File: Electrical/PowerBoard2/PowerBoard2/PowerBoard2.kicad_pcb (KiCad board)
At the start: 2 copper layers, 30 parts, among them U1 LMZ22005TZ/NOPB, U2 INA226AIDGSR, U4 TLV2370IDBVR, U5 TLV2370IDBVR

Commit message: pads
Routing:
- net /Buck Converter/Vin (12V): track 7.75 -> 14.7 mm
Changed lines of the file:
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@@
 	(footprint "Capacitor_SMD:C_0805_2012Metric_Pad1.18x1.45mm_HandSolder"
 		(layer "F.Cu")
-		(at 130.8 88.7375 90)
+		(at 130.8 88.75 90)
 		(descr "Capacitor SMD 0805 (2012 Metric), square (rectangular) end terminal, IPC_7351 nominal with elongated pad for handsoldering. (Body size source: IPC-SM-782 page 76, https://www.pcb-3d.com/wordpress/wp-content/uploads/ipc-sm-782a_amendment_1_and_2.pdf, https://docs.google.com/spreadsheets/d/1BsfQQcO9C6DZCsRaXUlFlo91Tg2WpOkGARC1WS5S8t0/edit?usp=sharing), generated with kicad-footprint-generator")
 		(tags "capacitor handsolder")
@@
 	(footprint "Capacitor_SMD:C_0805_2012Metric_Pad1.18x1.45mm_HandSolder"
 		(layer "F.Cu")
-		(at 128.2 88.7625 90)
+		(at 128.2 88.75 90)
 		(descr "Capacitor SMD 0805 (2012 Metric), square (rectangular) end terminal, IPC_7351 nominal with elongated pad for handsoldering. (Body size source: IPC-SM-782 page 76, https://www.pcb-3d.com/wordpress/wp-content/uploads/ipc-sm-782a_amendment_1_and_2.pdf, https://docs.google.com/spreadsheets/d/1BsfQQcO9C6DZCsRaXUlFlo91Tg2WpOkGARC1WS5S8t0/edit?usp=sharing), generated with kicad-footprint-generator")
 		(tags "capacitor handsolder")
@@
 	)
 	(segment
-		(start 135.6 67.5)
-		(end 135.6 70.3)
+		(start 128.6939 72.1061)
+		(end 128.6939 71.2)
 		(width 0.2)
 		(layer "F.Cu")
@@
 	)
 	(segment
-		(start 128.6939 72.1061)
-		(end 128.6939 71.2)
+		(start 128.6939 71.2)
+		(end 128.6939 69.0061)
 		(width 0.2)
 		(layer "F.Cu")
@@
 	)
 	(segment
+		(start 128.6939 69.0061)
+		(end 130.2 67.5)
+		(width 0.2)
+		(layer "F.Cu")
+		(net 2)
+	)
+	(segment
 		(start 127 74.85)
 		(end 127 73.8)
@@
 	)
 	(segment
+		(start 130.2 67.5)
+		(end 135.6 67.5)
+		(width 0.2)
+		(layer "F.Cu")
+		(net 2)
+	)
+	(segment
 		(start 149.6 76.307201)
 		(end 149.6 79.45)
@@
 	(segment
 		(start 140.7648 65.6)
-		(end 141.7 65.6)
+		(end 141.6 65.6)
 		(width 0.2)
 		(layer "F.Cu")
@@
 	)
 	(segment
-		(start 141.7 65.6)
-		(end 141.9 65.8)
+		(start 141.9 65.9)
+		(end 141.9 67.25)
 		(width 0.2)
 		(layer "F.Cu")
@@
 	)
 	(segment
-		(start 142.075002 67.500002)
+		(start 142.150002 67.500002)
 		(end 143 67.500002)
 		(width 0.2)
@@
 	)
 	(segment
-		(start 144.8 61.3)
-		(end 140.7648 65.3352)
+		(start 141.6 65.6)
+		(end 141.9 65.9)
 		(width 0.2)
 		(layer "F.Cu")
@@
 	)
 	(segment
-		(start 141.9 67.325)
-		(end 142.075002 67.500002)
+		(start 144.8 61.3)
+		(end 140.7648 65.3352)
 		(width 0.2)
 		(layer "F.Cu")
@@
 	)
 	(segment
-		(start 141.9 65.8)
-		(end 141.9 67.325)
+		(start 141.9 67.25)
+		(end 142.150002 67.500002)
 		(width 0.2)
 		(layer "F.Cu")
@@
 	)
 	(segment
-		(start 151.3648 65.6)
-		(end 151.3648 65.3648)
+		(start 152.4824 65.875001)
+		(end 152.4824 67.225001)
 		(width 0.2)
 		(layer "F.Cu")
@@
 	)
 	(segment
-		(start 152.3014 65.6)
-		(end 152.5 65.7986)
+		(start 151.3648 65.6)
+		(end 151.3648 65.3648)
 		(width 0.2)
 		(layer "F.Cu")
@@
 	)
 	(segment
-		(start 152.5 67.336602)
-		(end 152.6634 67.500002)
+		(start 152.1824 65.575001)
+		(end 152.4824 65.875001)
 		(width 0.2)
 		(layer "F.Cu")
@@
 	)
 	(segment
-		(start 152.5 65.7986)
-		(end 152.5 67.336602)
+		(start 151.3472 65.575001)
+		(end 152.1824 65.575001)
 		(width 0.2)
 		(layer "F.Cu")
@@
 	)
 	(segment
-		(start 151.3648 65.6)
-		(end 152.3014 65.6)
+		(start 151.3648 65.3648)
+		(end 147.3 61.3)
 		(width 0.2)
 		(layer "F.Cu")
@@
 	)
 	(segment
-		(start 151.3648 65.3648)
-		(end 147.3 61.3)
+		(start 152.757401 67.500002)
+		(end 153.6 67.500002)
 		(width 0.2)
 		(layer "F.Cu")
@@
 	)
 	(segment
-		(start 152.6634 67.500002)
-		(end 153.6 67.500002)
+		(start 152.4824 67.225001)
+		(end 152.757401 67.500002)
 		(width 0.2)
 		(layer "F.Cu")
@@
 		(polygon
 			(pts
-				(xy 154.5 81.5) (xy 160.5 81.5) (xy 162.6 79.4) (xy 162.6 77.4) (xy 161.2 76) (xy 159.5 76) (xy 153.3 69.8)
+				(xy 154.2 81.7) (xy 160.5 81.7) (xy 162.6 79.4) (xy 162.6 77.4) (xy 161.2 76) (xy 159.5 76) (xy 153.3 69.8)
 				(xy 127.8 69.8) (xy 127.8 72.6) (xy 130.9 72.6) (xy 135.8 77.5) (xy 140.5 77.5) (xy 143.5 74.5)
-				(xy 152.5 74.5) (xy 154.5 76.5)
+				(xy 152.5 74.5) (xy 154.2 76.5)
 			)
 		)
@@
 		(layer "F.Cu")
 		(hatch edge 0.5)
-		(priority 4)
 		(connect_pads yes
 			(clearance 0)
@@
 		(polygon
 			(pts
-				(xy 114.5 89.2) (xy 114.5 90.3) (xy 117.1 90.3) (xy 139.5 95.975003) (xy 139.5 93.5) (xy 139.5 90)
-				(xy 131.75 89.2)
+				(xy 147.5 81.7) (xy 147.5 78.9) (xy 145.3 76.8) (xy 145.3 75.6) (xy 144.3 75.6) (xy 141.5 78.4)
+				(xy 141.5 82.4) (xy 139 84.8) (xy 139 98) (xy 141.8 98) (xy 144.9 94.4) (xy 144.9 83.4)
 			)
 		)
@@
 		(layer "F.Cu")
 		(hatch edge 0.5)
+		(priority 1)
 		(connect_pads yes
 			(clearance 0)
@@
 		(polygon
 			(pts
-				(xy 139 98) (xy 141.5 98) (xy 145 94.5) (xy 145 83.5) (xy 146.8 81.7) (xy 147.5 81.7) (xy 147.5 79)
-				(xy 146 77.623433) (xy 145.348002 77) (xy 145.348002 76.5) (xy 145.348002 75.550801) (xy 143.949199 75.550801)
-				(xy 141.5 78) (xy 141.5 85.5) (xy 139 87.9)
+				(xy 141.8 98) (xy 142.9 99.4) (xy 160.96 99.4) (xy 162.6 98.1) (xy 162.6 95.6) (xy 160.849998 94.4)
+				(xy 144.9 94.4)
 			)
 		)
@@
 		(layer "F.Cu")
 		(hatch edge 0.5)
-		(priority 1)
+		(priority 4)
 		(connect_pads yes
 			(clearance 0)
@@
 		(polygon
 			(pts
-				(xy 141.25 97.75) (xy 142.9 99.4) (xy 160.96 99.4) (xy 162.6 98.1) (xy 162.6 95.6) (xy 160.849998 94.4)
-				(xy 144.6 94.4)
+				(xy 114.3 90.4) (xy 117.5 90.4) (xy 120.2 93.1) (xy 124 93.1) (xy 139 96) (xy 139 90) (xy 131.8 89.1)
+				(xy 114.3 89.1)
 			)
 		)

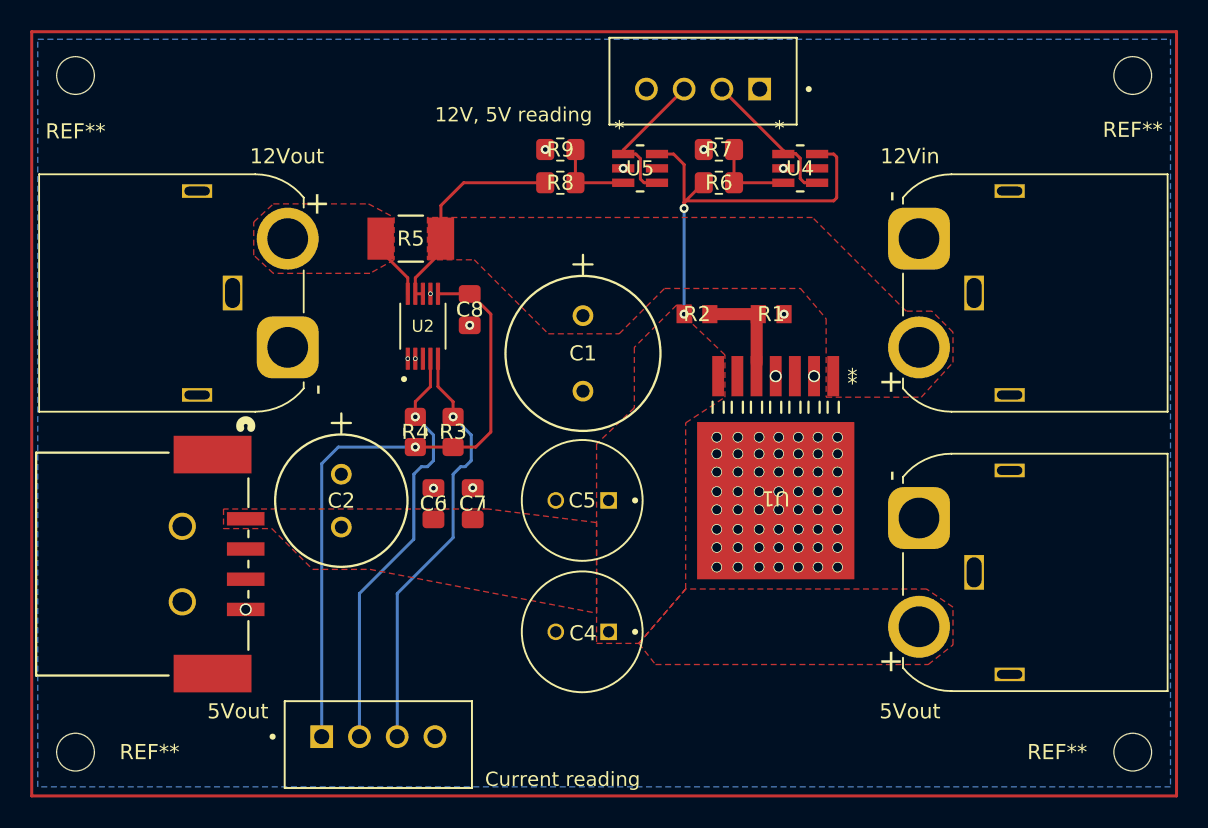
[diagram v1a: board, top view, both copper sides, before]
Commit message: Updated Board to use two INA226
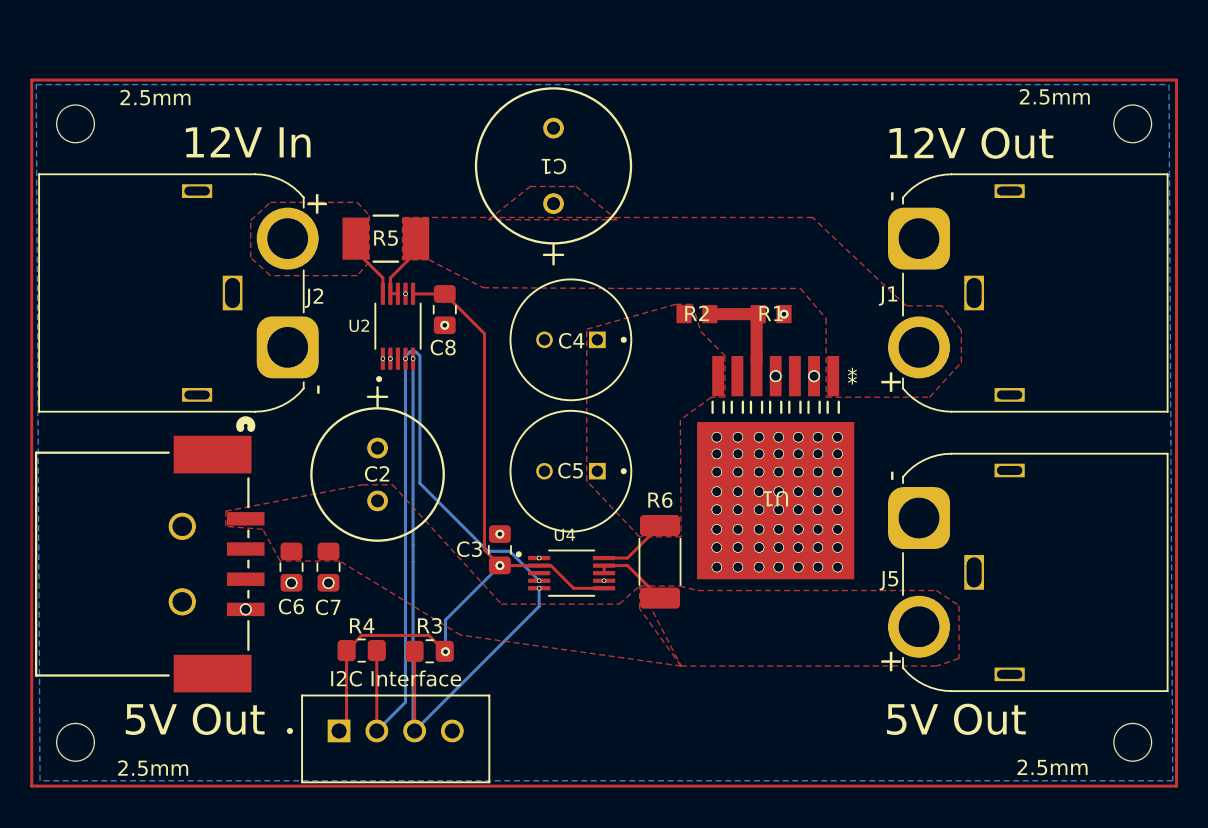
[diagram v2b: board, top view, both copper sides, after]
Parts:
- removed 12V, 5V reading: B4B-XH-A_LF__SN_, B4B-XH-A_LF__SN_:JST_B4B-XH-A_LF__SN_
- removed R7, R9: 33k, Resistor_SMD:R_0805_2012Metric_Pad1.20x1.40mm_HandSolder
- removed R8: 120k, Resistor_SMD:R_0805_2012Metric_Pad1.20x1.40mm_HandSolder
- removed REF** (x2): MountingHole_2.5mm, MountingHole:MountingHole_2.5mm
- removed U5: TLV2370IDBVR, _Footprints:DBV6
- added 2.5mm: MountingHole_2.5mm, MountingHole:MountingHole_2.5mm, F.Cu at (174.5, 63.6)
- added 2.5mm: MountingHole_2.5mm, MountingHole:MountingHole_2.5mm, F.Cu at (104.5, 63.6)
- added C3: 0.1uF, Capacitor_SMD:C_0805_2012Metric_Pad1.18x1.45mm_HandSolder, F.Cu at (132.6, 91.8)
- 5V Out: renamed from 5Vout
- I2C Interface: renamed from Current reading
- R6: value 36k -> CSNL2010FT2L00; footprint Resistor_SMD:R_0805_2012Metric_Pad1.20x1.40mm_HandSolder -> Resistor_SMD:R_2010_5025Metric_Pad1.40x2.65mm_HandSolder
- U4: value TLV2370IDBVR -> INA226AIDGSR; footprint _Footprints:DBV6 -> Libraries:INA226AIDGSR
- moved U4 30.8 mm to (137.3, 93.3)
- moved R6 25.4 mm to (143.2, 92.6), turned to 90 degrees
- moved C4 19.3 mm to (137.3, 77.9)
- moved R4 14.9 mm to (123.5, 98.5), turned to 0 degrees
- moved R3 14.6 mm to (128.0, 98.5), turned to 180 degrees
- moved C7 10.4 mm to (121.2, 93.0), turned to -90 degrees
- moved C6 10.3 mm to (118.8, 93.0), turned to -90 degrees
- moved C1 7.67 mm to (136.2, 68.9), turned to 90 degrees
- moved C2 2.96 mm to (124.5, 85.1)
- moved C5 2.07 mm to (137.3, 86.6)
- moved C8 1.65 mm to (128.9, 75.9)
- moved R5 1.65 mm to (125.0, 71.2)
- moved U2 1.65 mm to (125.8, 77.0)
- moved I2C Interface 1.21 mm to (125.7, 104.3)
- moved 2.5mm 0.65 mm to (104.5, 104.5)
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- renumbered REF** to 2.5mm, 12Vin to J1, 12Vout to J2, 5Vout to J5
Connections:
- C1 pad 1: /Buck Converter/Vin (12V) -> +12V
- C4 pad 1: +5V -> /Buck Converter/Vout (5V 5A)
- C5 pad 1: +5V -> /Buck Converter/Vout (5V 5A)
- J1 pad 2: /Buck Converter/Vin (12V) -> +12V
- J2 pad 2: +12V -> Net-(J2--)
- R2 pad 1: +5V -> /Buck Converter/Vout (5V 5A)
- R5 pad 1: +12V -> Net-(J2--)
- R5 pad 2: /Buck Converter/Vin (12V) -> +12V
- R6 pad 2: Net-(U4-IN+) -> /Buck Converter/Vout (5V 5A)
- U1 pad 1: /Buck Converter/Vin (12V) -> +12V
- U1 pad 7: +5V -> /Buck Converter/Vout (5V 5A)
- U2 pad 10: +12V -> Net-(J2--)
- U2 pad 8: /Buck Converter/Vin (12V) -> +12V
- U2 pad 9: /Buck Converter/Vin (12V) -> +12V
- U4 pad 1: Net-(U4-IN-) -> GND
- U4 pad 2: GND -> +3.3V
- U4 pad 3: Net-(U4-IN+) -> unconnected-(U4-ALERT-Pad3)
- U4 pad 4: Net-(U4-IN-) -> /SDA
- U4 pad 5: unconnected-(U4-*SHDN-Pad5) -> /SCL
- U4 pad 6: +5V -> +3.3V
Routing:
- net +5V: track 28.1 -> 5.09 mm, vias 2 -> 0
- net /SDA: track 28.2 -> 51.1 mm, vias 1 -> 2
- net /SCL: track 28.1 -> 42.8 mm, vias 1 -> 2
- net /Buck Converter/Vin (12V): track 14.7 -> 0.00 mm
- net Net-(U4-IN-): track 9.82 -> 0.00 mm
- net Net-(U5-IN-): track 9.78 -> 0.00 mm
- net +3.3V: track 42.0 -> 49.9 mm, vias 1 -> 2
- net Net-(U4-IN+): track 5.46 -> 0.00 mm
- net Net-(U5-IN+): track 5.36 -> 0.00 mm
- net /Buck Converter/Vout (5V 5A): track 0.00 -> 4.59 mm
- net Net-(J2--): track 0.00 -> 3.45 mm
- net GND: vias 70 -> 69
- added copper zone on F.Cu, net /Buck Converter/Vout (5V 5A)
- removed copper zone on F.Cu, net /Buck Converter/Vin (12V)
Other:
- board text added: "12V In"
- board text added: "12V Out"
- board text added: "5V Out"

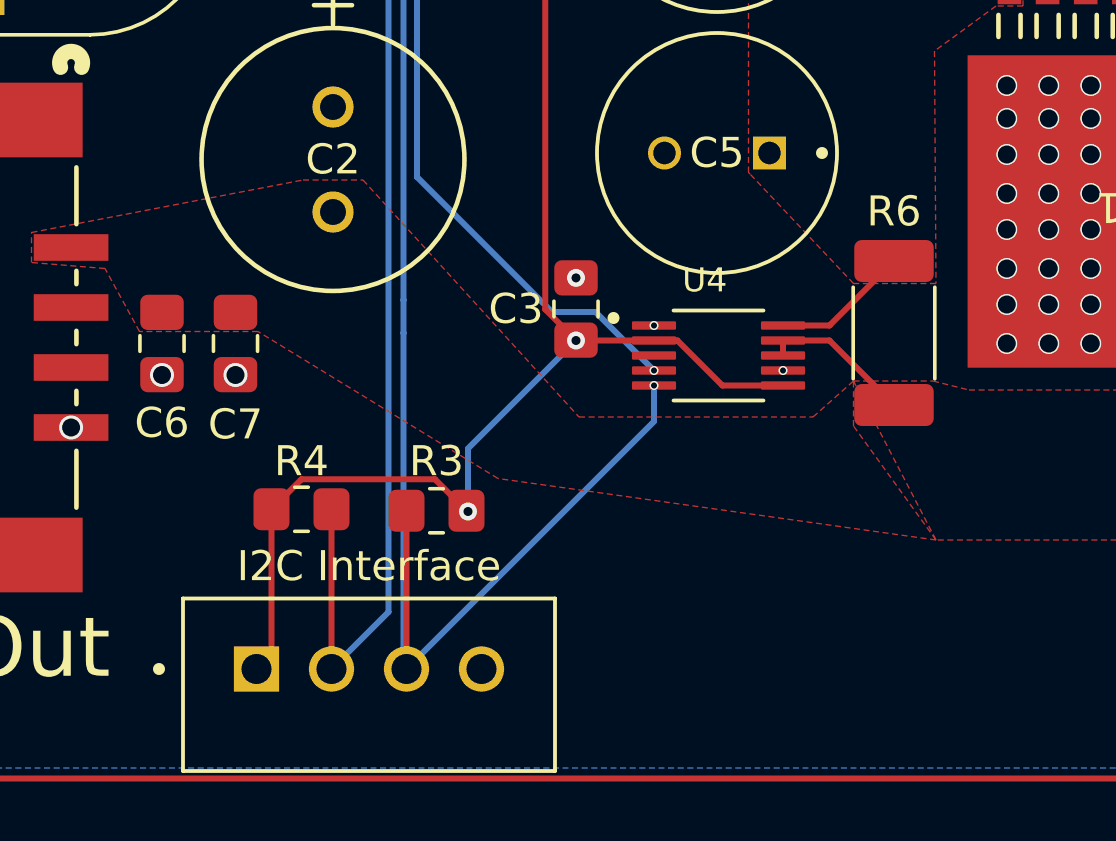
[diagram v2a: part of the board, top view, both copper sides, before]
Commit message: Updated Silkscreen
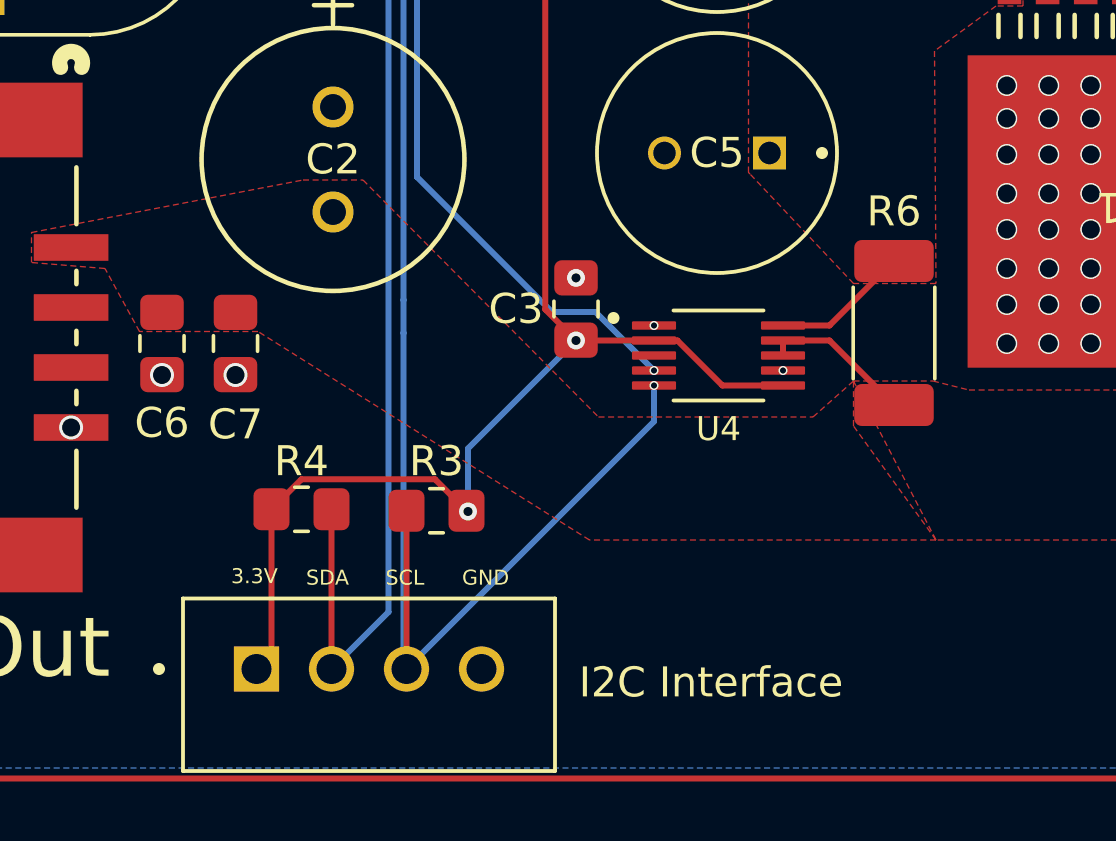
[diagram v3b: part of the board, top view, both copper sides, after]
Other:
- board text added: "3.3V"
- board text added: "GND"
- board text added: "SCL"
- board text added: "SDA"
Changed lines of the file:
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@@
 		(at 125.7 104.325 180)
 		(property "Reference" "I2C Interface"
-			(at 0 3.95 0)
+			(at -11.4 0.075 0)
 			(layer "F.SilkS")
 			(effects
@@
 		(at 137.35 93.35)
 		(property "Reference" "U4"
-			(at -0.46 -2.508 360)
+			(at 0 2.45 360)
 			(layer "F.SilkS")
 			(effects
@@
 		(layer "F.Cu")
 	)
+	(gr_text "3.3V"
+		(at 121.1 101 0)
+		(layer "F.SilkS")
+		(effects
+			(font
+				(size 0.5 0.5)
+				(thickness 0.1)
+			)
+			(justify left bottom)
+		)
+	)
 	(gr_text "12V In"
 		(at 115.9 64.9 0)
@@
 		)
 	)
+	(gr_text "GND"
+		(at 128.8 101.05 0)
+		(layer "F.SilkS")
+		(effects
+			(font
+				(size 0.5 0.5)
+				(thickness 0.1)
+			)
+			(justify left bottom)
+		)
+	)
 	(gr_text "5V Out\n"
 		(at 162.75 103.1 0)
@@
 		)
 	)
+	(gr_text "SDA"
+		(at 123.6 101.05 0)
+		(layer "F.SilkS")
+		(effects
+			(font
+				(size 0.5 0.5)
+				(thickness 0.1)
+			)
+			(justify left bottom)
+		)
+	)
+	(gr_text "SCL"
+		(at 126.25 101.05 0)
+		(layer "F.SilkS")
+		(effects
+			(font
+				(size 0.5 0.5)
+				(thickness 0.1)
+			)
+			(justify left bottom)
+		)
+	)
 	(via
 		(at 154.96 86.65)
@@
 		(polygon
 			(pts
-				(xy 114.45 89.25) (xy 123.5 87.5) (xy 125.5 87.5) (xy 132.7 95.4) (xy 140.5 95.4) (xy 141.85 94.2)
-				(xy 144.6 99.5) (xy 130 97.45) (xy 122 92.55) (xy 118.05 92.55) (xy 116.9 90.45) (xy 114.45 90.25)
+				(xy 114.45 89.25) (xy 123.5 87.5) (xy 125.5 87.5) (xy 133.35 95.4) (xy 140.5 95.4) (xy 141.85 94.2)
+				(xy 144.6 99.5) (xy 133.05 99.5) (xy 122 92.55) (xy 118.05 92.55) (xy 116.9 90.45) (xy 114.45 90.25)
 			)
 		)

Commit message: Fixed Filled Zones on PCB
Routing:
- added copper zone on F.Cu, net Net-(J2--)
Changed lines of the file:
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@@
 		(tags "mounting hole 2.5mm no annular")
 		(property "Reference" "2.5mm"
-			(at 5.15 1.75 360)
+			(at 5.15 1.75 0)
 			(layer "F.SilkS")
 			(effects
@@
 		)
 		(property "Value" "MountingHole_2.5mm"
-			(at 0 3.5 360)
+			(at 0 3.5 0)
 			(layer "F.Fab")
 			(effects
@@
 		)
 		(fp_text user "${REFERENCE}"
-			(at 0 0 360)
+			(at 0 0 0)
 			(layer "F.Fab")
 			(effects
@@
 		)
 		(property "Value" "25SEK120M"
-			(at 8.89 5.005 360)
+			(at 8.89 5.005 0)
 			(layer "F.Fab")
 			(effects
@@
 		)
 		(property "Footprint" "Libraries:25SEK120M"
-			(at 0 0 360)
+			(at 0 0 0)
 			(layer "F.Fab")
 			(hide yes)
@@
 		)
 		(property "Datasheet" ""
-			(at 0 0 360)
+			(at 0 0 0)
 			(layer "F.Fab")
 			(hide yes)
@@
 		)
 		(property "Description" ""
-			(at 0 0 360)
+			(at 0 0 0)
 			(layer "F.Fab")
 			(hide yes)
@@
 		(tags "mounting hole 2.5mm no annular")
 		(property "Reference" "2.5mm"
-			(at -5.3 1.7 360)
+			(at -5.3 1.7 0)
 			(layer "F.SilkS")
 			(effects
@@
 		)
 		(property "Value" "MountingHole_2.5mm"
-			(at 0 3.5 360)
+			(at 0 3.5 0)
 			(layer "F.Fab")
 			(effects
@@
 		)
 		(fp_text user "${REFERENCE}"
-			(at 0 0 360)
+			(at 0 0 0)
 			(layer "F.Fab")
 			(effects
@@
 		)
 		(property "Value" "25SEK120M"
-			(at 8.89 5.005 360)
+			(at 8.89 5.005 0)
 			(layer "F.Fab")
 			(effects
@@
 		)
 		(property "Footprint" "Libraries:25SEK120M"
-			(at 0 0 360)
+			(at 0 0 0)
 			(layer "F.Fab")
 			(hide yes)
@@
 		)
 		(property "Datasheet" ""
-			(at 0 0 360)
+			(at 0 0 0)
 			(layer "F.Fab")
 			(hide yes)
@@
 		)
 		(property "Description" ""
-			(at 0 0 360)
+			(at 0 0 0)
 			(layer "F.Fab")
 			(hide yes)
@@
 		(at 137.35 93.35)
 		(property "Reference" "U4"
-			(at 0 2.45 360)
+			(at 0 2.45 0)
 			(layer "F.SilkS")
 			(effects
@@
 		)
 		(property "Value" "INA226AIDGSR"
-			(at 5.636 2.508 360)
+			(at 5.636 2.508 0)
 			(layer "F.Fab")
 			(effects
@@
 		)
 		(property "Footprint" "Libraries:INA226AIDGSR"
-			(at 0 0 360)
+			(at 0 0 0)
 			(layer "F.Fab")
 			(hide yes)
@@
 		)
 		(property "Datasheet" ""
-			(at 0 0 360)
+			(at 0 0 0)
 			(layer "F.Fab")
 			(hide yes)
@@
 		)
 		(property "Description" ""
-			(at 0 0 360)
+			(at 0 0 0)
 			(layer "F.Fab")
 			(hide yes)
@@
 	)
 	(zone
-		(net 10)
-		(net_name "+12V")
+		(net 15)
+		(net_name "Net-(J2--)")
 		(layer "F.Cu")
 		(hatch edge 0.5)
@@
 			(pts
 				(xy 154.2 81.7) (xy 161.05 81.7) (xy 163.15 79.4) (xy 163.15 77.25) (xy 161.85 75.65) (xy 159.5 75.65)
-				(xy 153.3 69.8) (xy 126.15 69.8) (xy 126.15 72.6) (xy 127.9 72.6) (xy 127.9 72.6) (xy 131.5 74.45)
-				(xy 141 74.5) (xy 152.5 74.5) (xy 154.2 76.5)
+				(xy 153.3 69.8) (xy 126.15 69.8) (xy 126.15 72.6) (xy 127.9 72.6) (xy 131.5 74.45) (xy 141 74.5)
+				(xy 152.5 74.5) (xy 154.2 76.5)
 			)
 		)
